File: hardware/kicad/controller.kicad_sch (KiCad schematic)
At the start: 30 parts, among them J1 Data, J2 Power, U1 AP1117-50, U4 TS924, U5 TS924, U7 TS924, U8 TS924

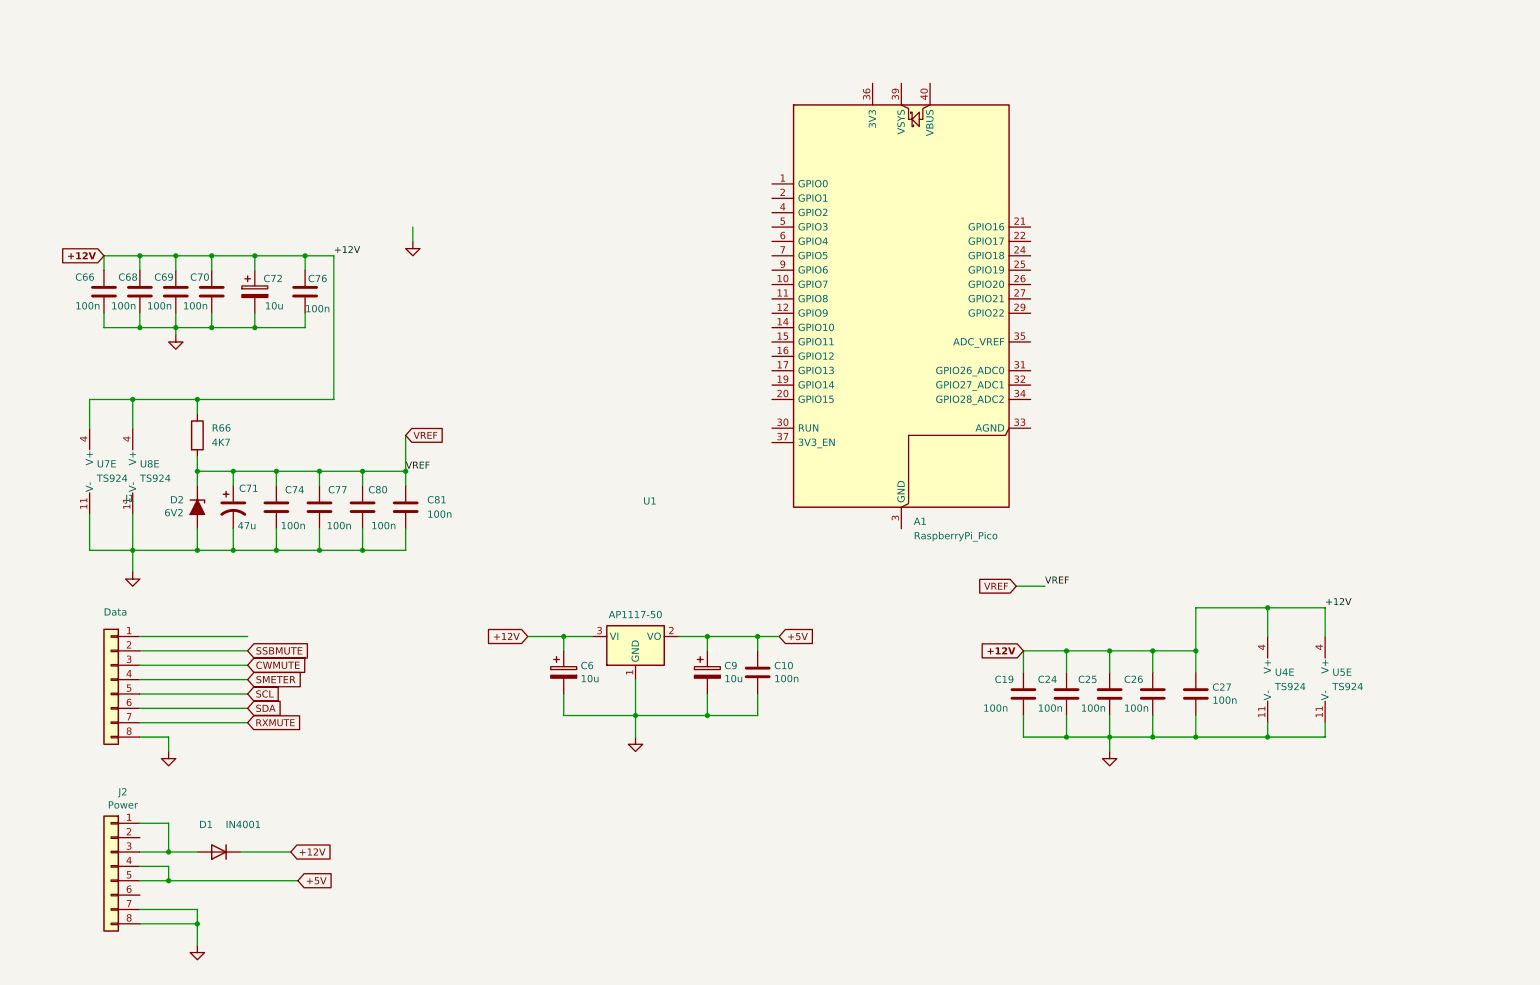
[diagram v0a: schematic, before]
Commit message: Document SSC notes reference in CURRENT_SI5351_APPROACH.md
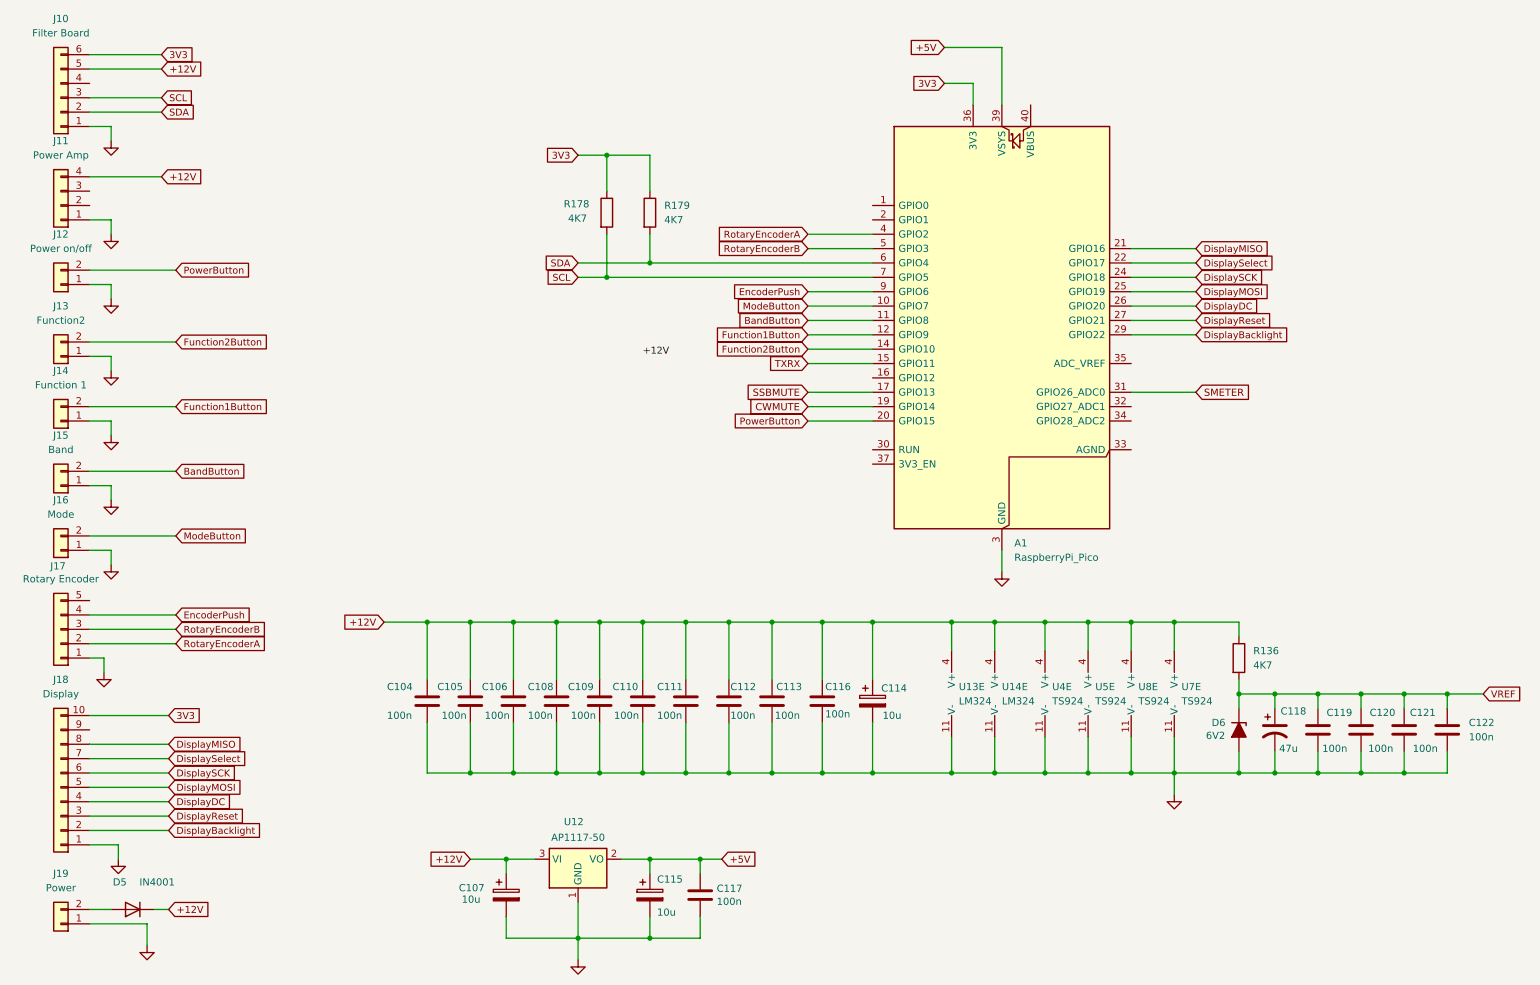
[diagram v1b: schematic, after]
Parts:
- removed J1: Data, Connector_PinHeader_2.54mm:PinHeader_1x08_P2.54mm_Vertical, symbol Connector_Generic:Conn_01x08
- removed J2: Power, Connector_PinHeader_2.54mm:PinHeader_1x08_P2.54mm_Vertical, symbol Connector_Generic:Conn_01x08
- added J10: Filter Board, symbol Connector_Generic:Conn_01x06
- added J11: Power Amp, symbol Connector_Generic:Conn_01x04
- added J12: Power on/off, symbol Connector_Generic:Conn_01x02
- added J13: Function2, symbol Connector_Generic:Conn_01x02
- added J14: Function 1, symbol Connector_Generic:Conn_01x02
- added J15: Band, symbol Connector_Generic:Conn_01x02
- added J16: Mode, symbol Connector_Generic:Conn_01x02
- added J17: Rotary Encoder, symbol Connector_Generic:Conn_01x05
- added J18: Display, symbol Connector_Generic:Conn_01x10
- added J19: Power, symbol Connector_Generic:Conn_01x02
- added R178, R179: 4K7, symbol Device:R
- added U13, U14: LM324, symbol Amplifier_Operational:LM324
- renumbered C19 to C104, C66 to C105, C24 to C106, C6 to C107, C68 to C108, C25 to C109, C69 to C110, C26 to C111, C70 to C112, C27 to C113, C72 to C114, C9 to C115, C76 to C116, C10 to C117, C71 to C118, C74 to C119, C77 to C120, C80 to C121, C81 to C122, D1 to D5, D2 to D6, R66 to R136, U1 to U12, U8 to U7, U7 to U8
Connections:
- net +12V: now also J10.5 (Pin_5), J11.4 (Pin_4), U13.4 (V+), U14.4 (V+)
- net +5V: now also A1.39 (VSYS)
- net CWMUTE: now also A1.19 (GPIO14)
- net GND: now also A1.13 (GND), A1.18 (GND), A1.23 (GND), A1.28 (GND), A1.3 (GND), A1.38 (GND), A1.8 (GND), J10.1 (Pin_1), J11.1 (Pin_1), J12.1 (Pin_1), J13.1 (Pin_1), J14.1 (Pin_1), J15.1 (Pin_1), J16.1 (Pin_1), J17.1 (Pin_1), J18.1 (Pin_1), J19.1 (Pin_1), U13.11 (V-), U14.11 (V-)
- net SCL: now also A1.7 (GPIO5), J10.3 (Pin_3), R178.2
- net SDA: now also A1.6 (GPIO4), J10.2 (Pin_2), R179.2
- net SMETER: now also A1.31 (GPIO26_ADC0)
- net SSBMUTE: now also A1.17 (GPIO13)
- net at D5.2 (A): now also J19.2 (Pin_2)
- net ModeButton: now reaches A1.10 (GPIO7)
- net ModeButton: now also J16.2 (Pin_2)
- net BandButton: now reaches A1.11 (GPIO8)
- net BandButton: now also J15.2 (Pin_2)
- net Function1Button: now reaches A1.12 (GPIO9)
- net Function1Button: now also J14.2 (Pin_2)
- net Function2Button: now reaches A1.14 (GPIO10)
- net Function2Button: now also J13.2 (Pin_2)
- net TXRX: now reaches A1.15 (GPIO11)
- net PowerButton: now reaches A1.20 (GPIO15)
- net PowerButton: now also J12.2 (Pin_2)
- net DisplayMISO: now reaches A1.21 (GPIO16)
- net DisplayMISO: now also J18.8 (Pin_8)
- net DisplaySelect: now reaches A1.22 (GPIO17)
- net DisplaySelect: now also J18.7 (Pin_7)
- net DisplaySCK: now reaches A1.24 (GPIO18)
- net DisplaySCK: now also J18.6 (Pin_6)
- net DisplayMOSI: now reaches A1.25 (GPIO19)
- net DisplayMOSI: now also J18.5 (Pin_5)
- net DisplayDC: now reaches A1.26 (GPIO20)
- net DisplayDC: now also J18.4 (Pin_4)
- net DisplayReset: now reaches A1.27 (GPIO21)
- net DisplayReset: now also J18.3 (Pin_3)
- net DisplayBacklight: now reaches A1.29 (GPIO22)
- net DisplayBacklight: now also J18.2 (Pin_2)
- net 3V3: now reaches A1.36 (3V3)
- net 3V3: now also J10.6 (Pin_6), J18.10 (Pin_10), R178.1, R179.1
- net RotaryEncoderA: now reaches A1.4 (GPIO2)
- net RotaryEncoderA: now also J17.2 (Pin_2)
- net RotaryEncoderB: now reaches A1.5 (GPIO3)
- net RotaryEncoderB: now also J17.3 (Pin_3)
- net EncoderPush: now reaches A1.9 (GPIO6)
- net EncoderPush: now also J17.4 (Pin_4)
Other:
- moved on the sheet: A1, C104, C105, C106, C107, C108, C109, C110, C111, C112, C113, C114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
